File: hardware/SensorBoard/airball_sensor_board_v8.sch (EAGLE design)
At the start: 63 parts, among them IC1 CP2102, J5 105450-0101, T1 BC846, T2 BC846, U1 BQ24075, U2 BQ27441-G1, U3 BMP390, U4 ESP-WROOM-32, U7 SP0503BAHT

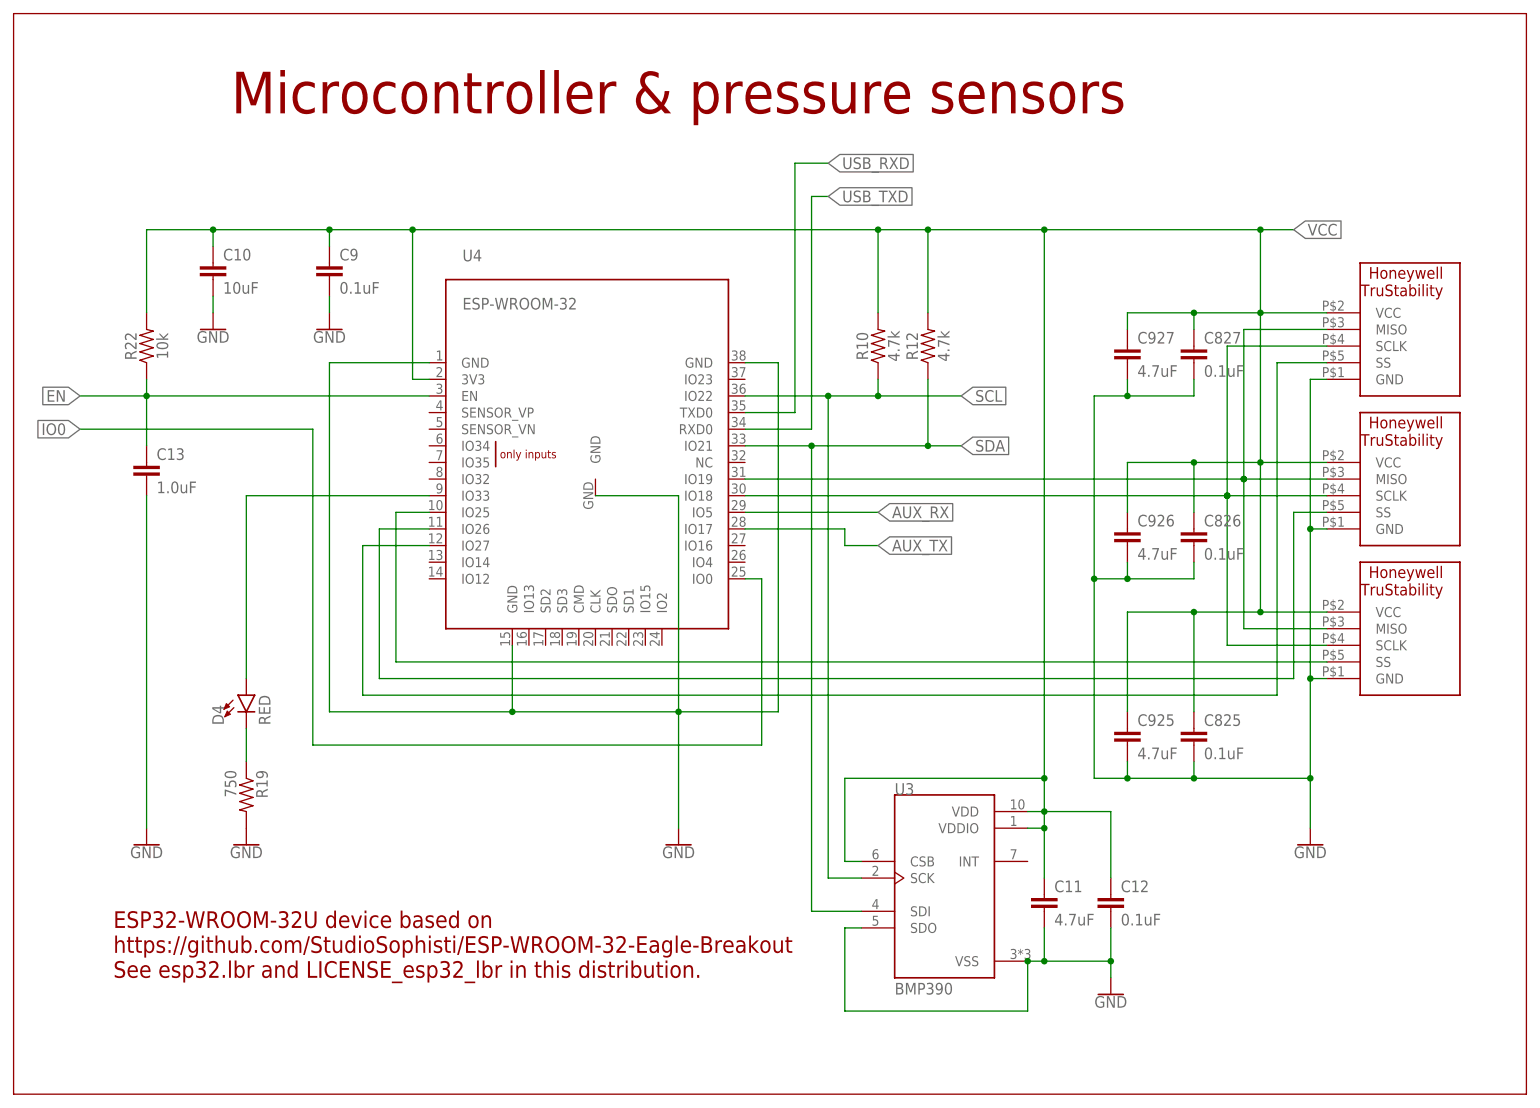
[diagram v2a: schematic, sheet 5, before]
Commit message: Added QWIIC I2C connector and rearranged a bit.
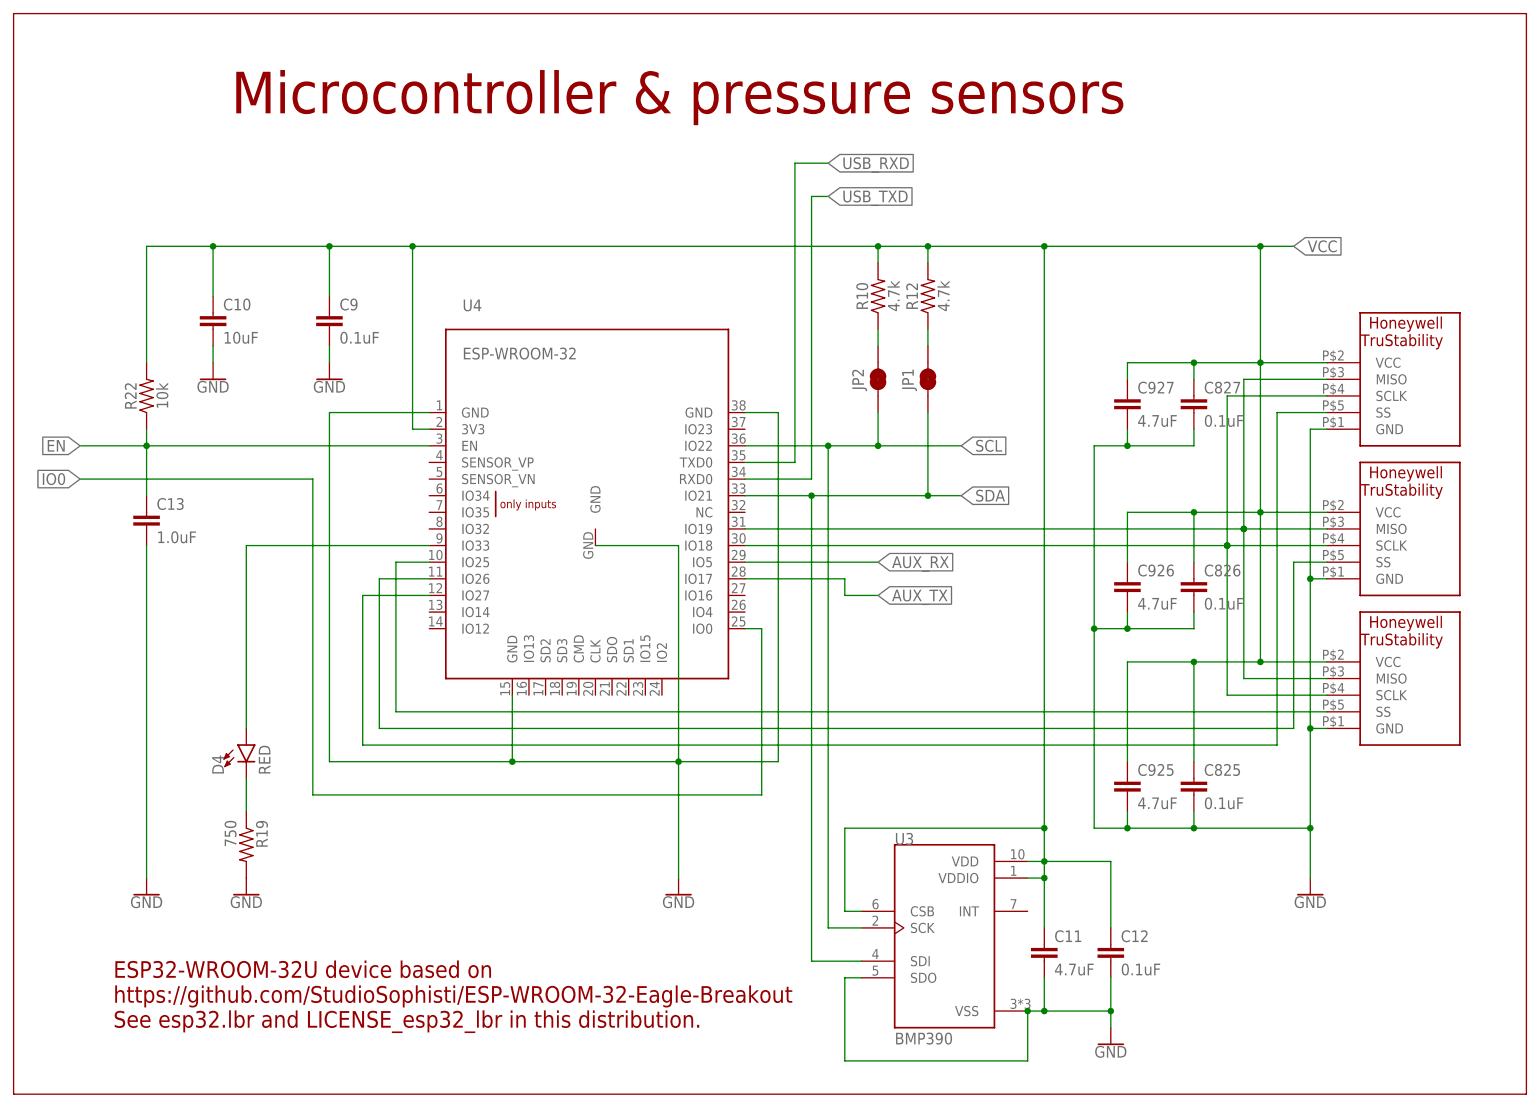
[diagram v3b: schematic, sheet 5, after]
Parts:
- removed J1: (no value), SparkFun-Connectors:CONN_04PTH
- added J2: QWIIC_RIGHT_ANGLE, SparkFun-Connectors:QWIIC_CONNECTORJS-1MM
- added JP1, JP2: JUMPER-SMT_2_NC_TRACE_SILK, SparkFun-Jumpers:JUMPER-SMT_2_NC_TRACE_SILK
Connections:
- new net N$3: JP2.2, R10.1
- new net N$9: JP1.2, R12.1
- net GND: now also J2.1; no longer J1.1
- net SCL: now also J2.4, JP2.1; no longer J1.4, R10.1
- net SDA: now also J2.3, JP1.1; no longer J1.3, R12.1
- net VCC: now also J2.2; no longer J1.2
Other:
- moved on the sheet: C10, C11, C12, C13, C825, C826, C827, C9, C925, C926, C927, D4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
